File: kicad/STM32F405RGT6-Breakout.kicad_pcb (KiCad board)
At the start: 4 copper layers, 71.9 x 57 mm, 56 parts, among them J1 USB_C_Receptacle_USB2.0, J2 Uno Power, J3 SWD/JTAG, J4 Uno Analog, J5 Uno Digital 2, J6 Uno Digital 1, Q1 Si2301CDS, SW1 TS-1187A-B-A-B, SW2 TS-1187A-B-A-B, U1 STM32F405RGT6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

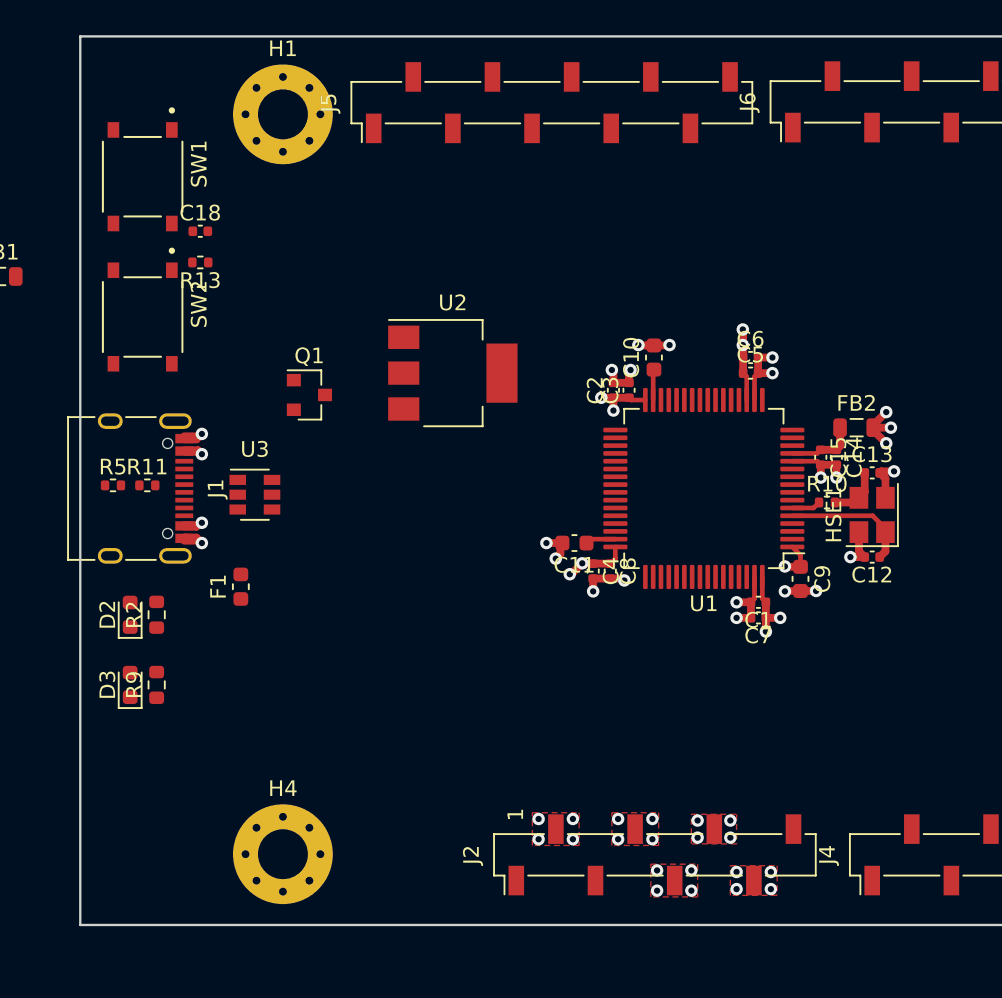
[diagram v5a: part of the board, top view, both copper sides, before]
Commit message: lol, I learned what thermal relief is
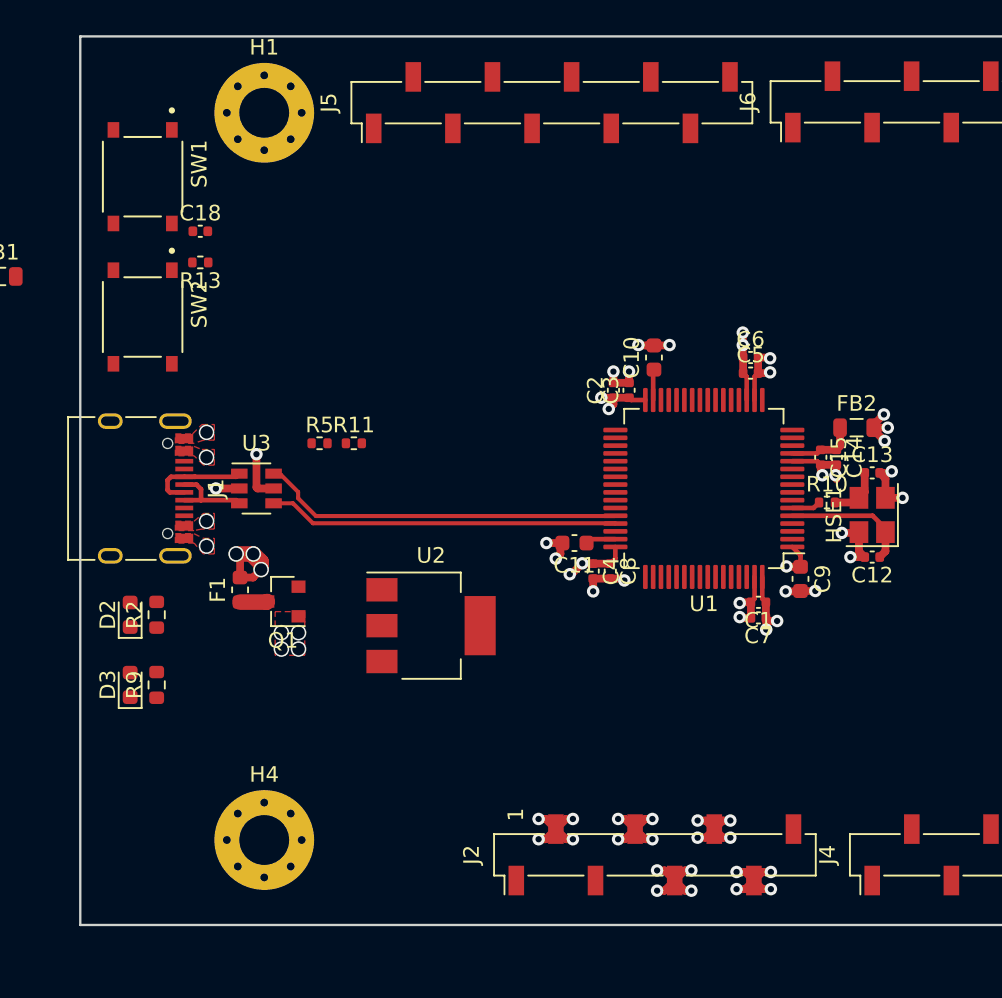
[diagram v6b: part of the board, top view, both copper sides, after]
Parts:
- moved U2 16.3 mm to (133.5, 107.2)
- moved R11 13.5 mm to (128.5, 95.5)
- moved R5 13.5 mm to (126.3, 95.5)
- moved Q1 13.4 mm to (124.0, 105.6), turned to 180 degrees
- moved H4 1.51 mm to (122.8, 120.9)
- moved H1 1.20 mm to (122.8, 74.3)
- moved U3 0.41 mm to (122.3, 98.4)
- moved F1 0.21 mm to (121.2, 104.9)
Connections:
- D1 pad 1: Net-(D1-Pad1) -> +5V
- F1 pad 2: +5V -> VBUS
- FB1 pad 2: Net-(D1-Pad1) -> +5V
- J1 pad A4: +5V -> VBUS
- J1 pad A9: +5V -> VBUS
- J1 pad B4: +5V -> VBUS
- J1 pad B9: +5V -> VBUS
- Q1 pad 1: Net-(D1-Pad1) -> +5V
- U3 pad 5: +5V -> VBUS
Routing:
- net USB_D-: track 0.00 -> 23.3 mm
- net USB_D+: track 0.00 -> 22.5 mm
- net VBUS: track 0.00 -> 10.8 mm, vias 0 -> 6
- net +3V3: track 24.7 -> 33.8 mm
- net GND: track 38.8 -> 46.3 mm, vias 28 -> 31
- net USB_CONN_D-: track 0.00 -> 6.54 mm
- net USB_CONN_D+: track 0.00 -> 5.52 mm
- net Net-(F1-Pad1): track 0.00 -> 1.77 mm
- net +5V: track 4.85 -> 5.48 mm, vias 6 -> 8
- added copper zone on F.Cu, net VBUS
- added copper zone on In2.Cu, net VBUS
- removed copper zone on F.Cu, net +3V3
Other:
- board text added: "3V3"
- board text added: "5V"
- board text added: "VBUS"

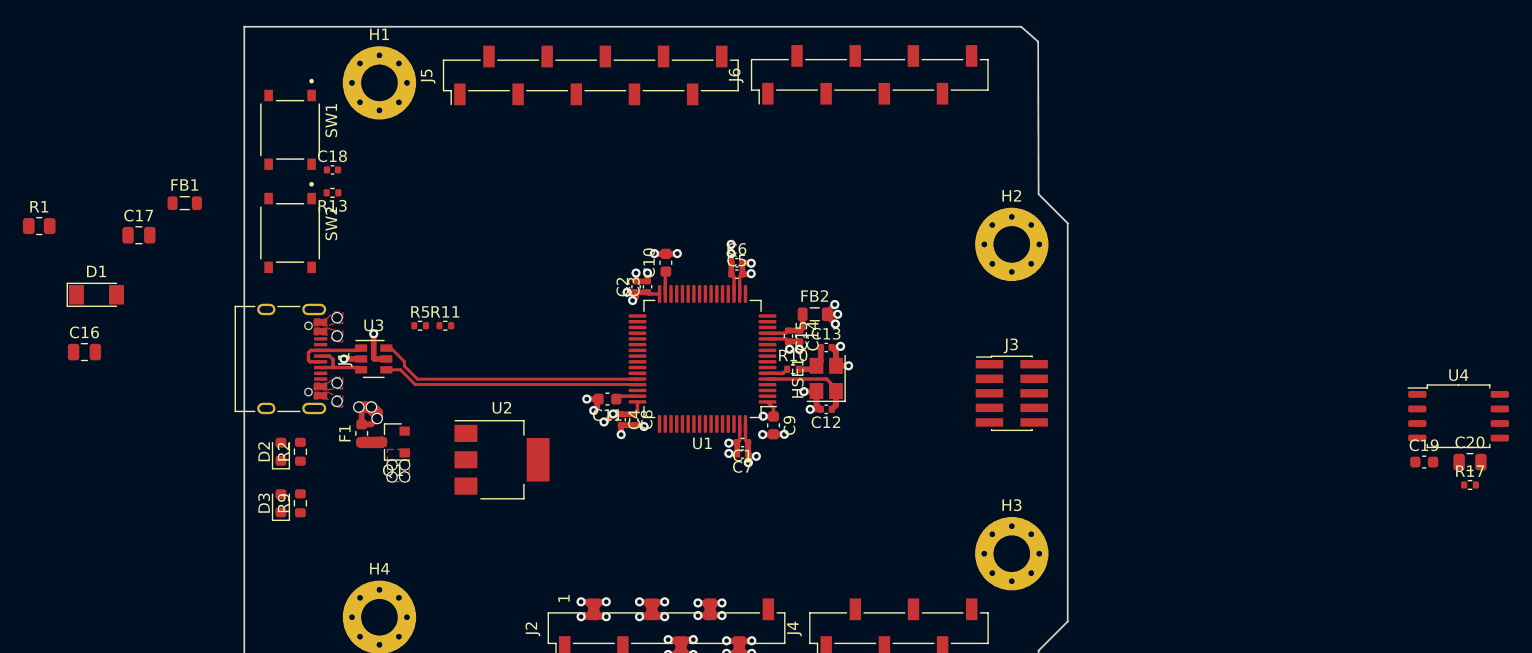
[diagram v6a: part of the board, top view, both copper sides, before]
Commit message: SPI flash routed
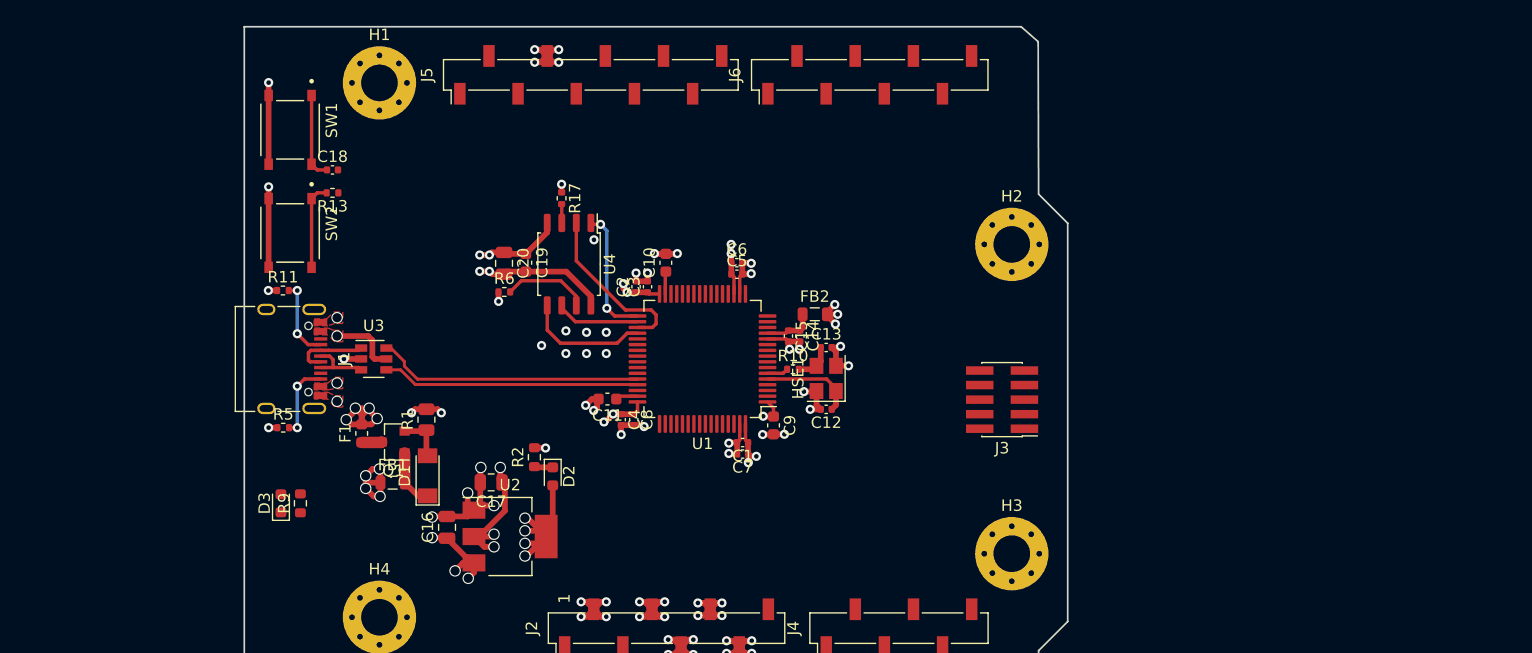
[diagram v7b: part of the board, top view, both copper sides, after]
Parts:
- added R6: 10k, Resistor_SMD:R_0402_1005Metric, F.Cu at (133.7, 92.5)
- moved C20 86.1 mm to (133.7, 90.0), turned to 270 degrees
- moved R17 83.2 mm to (138.7, 84.3), turned to 270 degrees
- moved C19 80.3 mm to (135.6, 90.0), turned to 270 degrees
- moved U4 78.8 mm to (139.3, 90.1), turned to 270 degrees
- moved R1 37.8 mm to (126.9, 103.7), turned to 90 degrees
- moved C17 37.6 mm to (132.5, 109.1), turned to 180 degrees
- moved C16 35.2 mm to (128.7, 113.1), turned to 90 degrees
- moved D1 32.9 mm to (127.0, 108.6), turned to 90 degrees
- moved FB1 30.4 mm to (123.9, 109.2)
- moved D2 23.8 mm to (137.9, 108.6), turned to 270 degrees
- moved R2 20.4 mm to (136.3, 106.9)
- moved R5 14.9 mm to (114.4, 104.4)
- moved R11 14.5 mm to (114.4, 92.4)
- moved U2 6.74 mm to (134.2, 113.9)
- moved J3 1.01 mm to (177.1, 101.9), turned to 180 degrees
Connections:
- C16 pad 1: Net-(C16-Pad1) -> +5V
- D1 pad 1: +5V -> Net-(D1-Pad1)
- FB1 pad 1: Net-(C16-Pad1) -> +5V
- FB1 pad 2: +5V -> Net-(D1-Pad1)
- Q1 pad 1: +5V -> Net-(D1-Pad1)
- U2 pad 3: Net-(C16-Pad1) -> +5V
- U4 pad 7: Net-(R17-Pad2) -> Net-(R6-Pad2)
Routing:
- net +3V3: track 33.8 -> 82.0 mm, vias 20 -> 30
- net GND: track 46.3 -> 85.9 mm, vias 31 -> 57
- net +5V: track 5.48 -> 22.1 mm, vias 8 -> 11
- net FLASH_MISO: track 0.00 -> 14.8 mm
- net FLASH_CS: track 0.00 -> 11.4 mm, vias 0 -> 2
- net FLASH_MOSI: track 0.00 -> 10.9 mm
- net NRST: track 0.00 -> 7.55 mm
- net Net-(R6-Pad2): track 0.00 -> 7.54 mm
- net Net-(R13-Pad2): track 0.00 -> 7.52 mm
- net FLASH_SCK: track 0.00 -> 7.34 mm
- net Net-(J1-PadA5): track 0.00 -> 6.95 mm, vias 0 -> 2
- net Net-(J1-PadB5): track 0.00 -> 6.64 mm, vias 0 -> 2
- net Net-(D1-Pad1): track 0.00 -> 5.07 mm
- net VBUS: track 10.8 -> 15.6 mm
- net Net-(D1-Pad2): track 0.00 -> 4.22 mm
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- removed copper zone on F.Cu, net +5V
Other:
- board text removed: "SPI"

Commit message: First ever attempt at actual routing, it went terribly
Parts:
- moved R7 105.0 mm to (120.9, 82.8), turned to 270 degrees
- moved R8 76.7 mm to (145.2, 88.0), turned to 90 degrees
- moved R3 59.8 mm to (150.8, 106.4), turned to 90 degrees
- moved R4 57.5 mm to (151.8, 106.4), turned to 90 degrees
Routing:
- net NRST: track 7.55 -> 105.5 mm, vias 0 -> 6
- net I2C1_SDA: track 0.00 -> 93.6 mm, vias 0 -> 3
- net I2C1_SCL: track 0.00 -> 90.9 mm, vias 0 -> 3
- net USART6_RX: track 0.00 -> 53.7 mm, vias 0 -> 2
- net SWO: track 0.00 -> 52.6 mm, vias 0 -> 2
- net USART6_TX: track 0.00 -> 46.4 mm, vias 0 -> 2
- net BOOT0: track 0.00 -> 46.0 mm, vias 0 -> 2
- net +3.3VA: track 4.44 -> 48.6 mm, vias 0 -> 2
- net SWDIO: track 0.00 -> 41.8 mm, vias 0 -> 2
- net GPIO_PA0: track 0.00 -> 41.0 mm, vias 0 -> 2
- net SWCLK: track 0.00 -> 40.1 mm, vias 0 -> 2
- net GPIO_PA2: track 0.00 -> 37.5 mm
- net SPI1_MISO: track 0.00 -> 33.2 mm, vias 0 -> 2
- net GPIO_PA1: track 0.00 -> 32.3 mm, vias 0 -> 2
- net GPIO_PA3: track 0.00 -> 31.6 mm, vias 0 -> 3
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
